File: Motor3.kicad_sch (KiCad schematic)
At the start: 53 parts, among them J601 Step Out, J604 Direction, J605 Direction, Q601 WSF07N10, Q602 WSF07N10, Q603 WSF07N10, Q604 WSF07N10, Q605 WSF07N10, Q606 WSF07N10, Q607 WSF07N10, Q608 WSF07N10

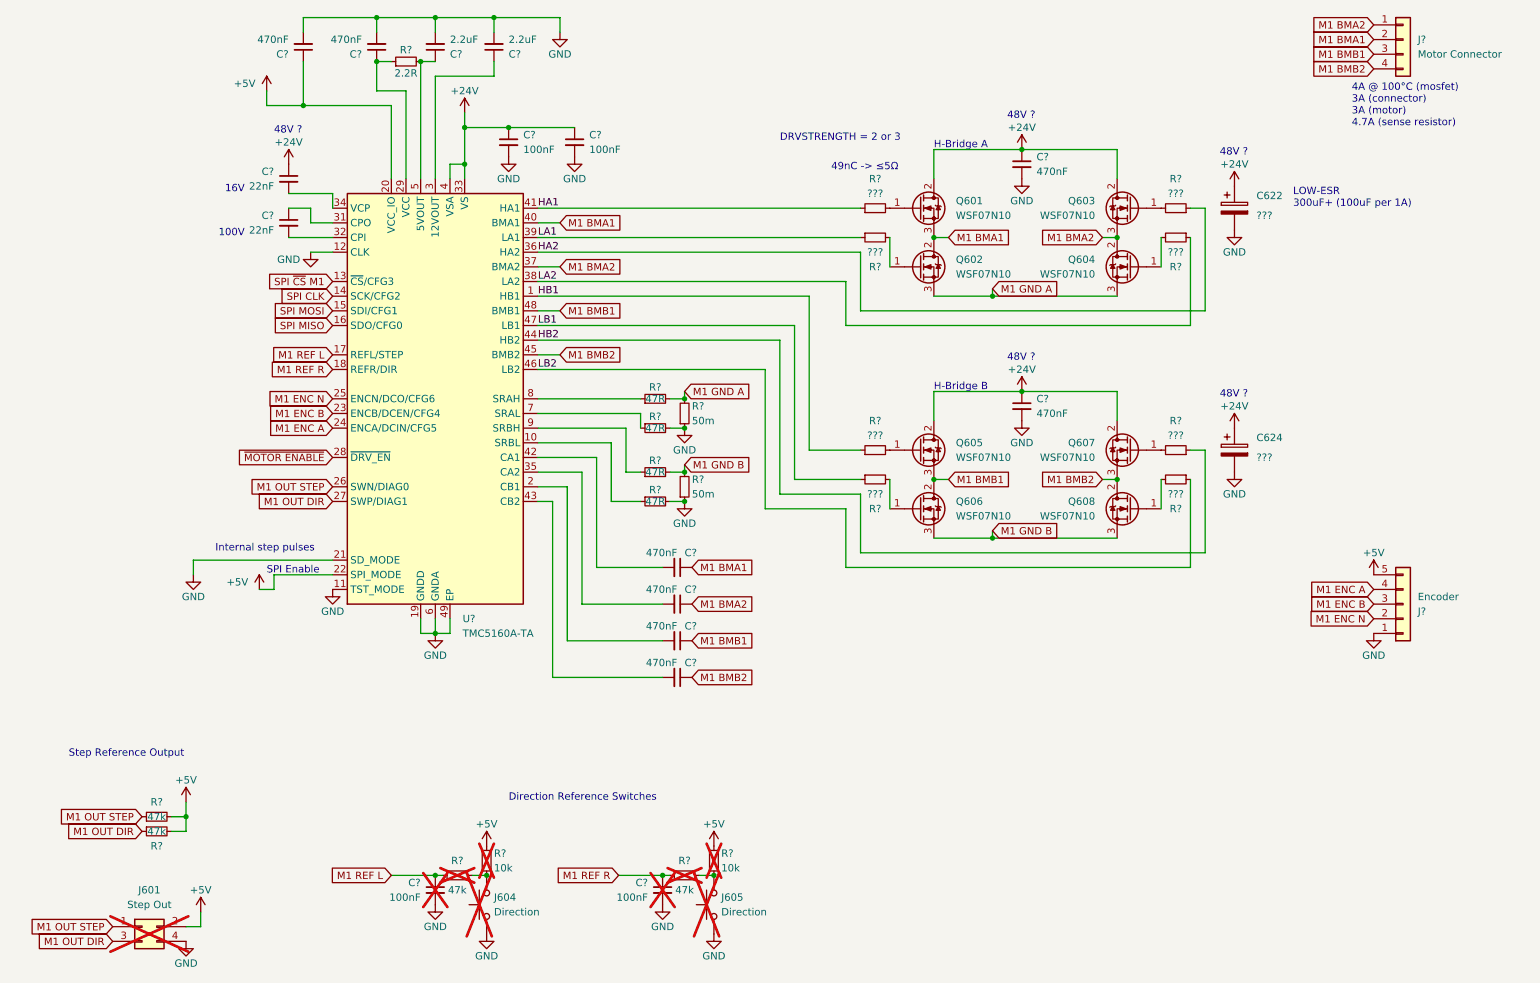
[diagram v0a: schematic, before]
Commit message: Assigning a lot of values to components Change MOSFETS for different (correct) ones Copy Motor1 to Motor2-4 Guess max current per voltage on PowerSupply schema
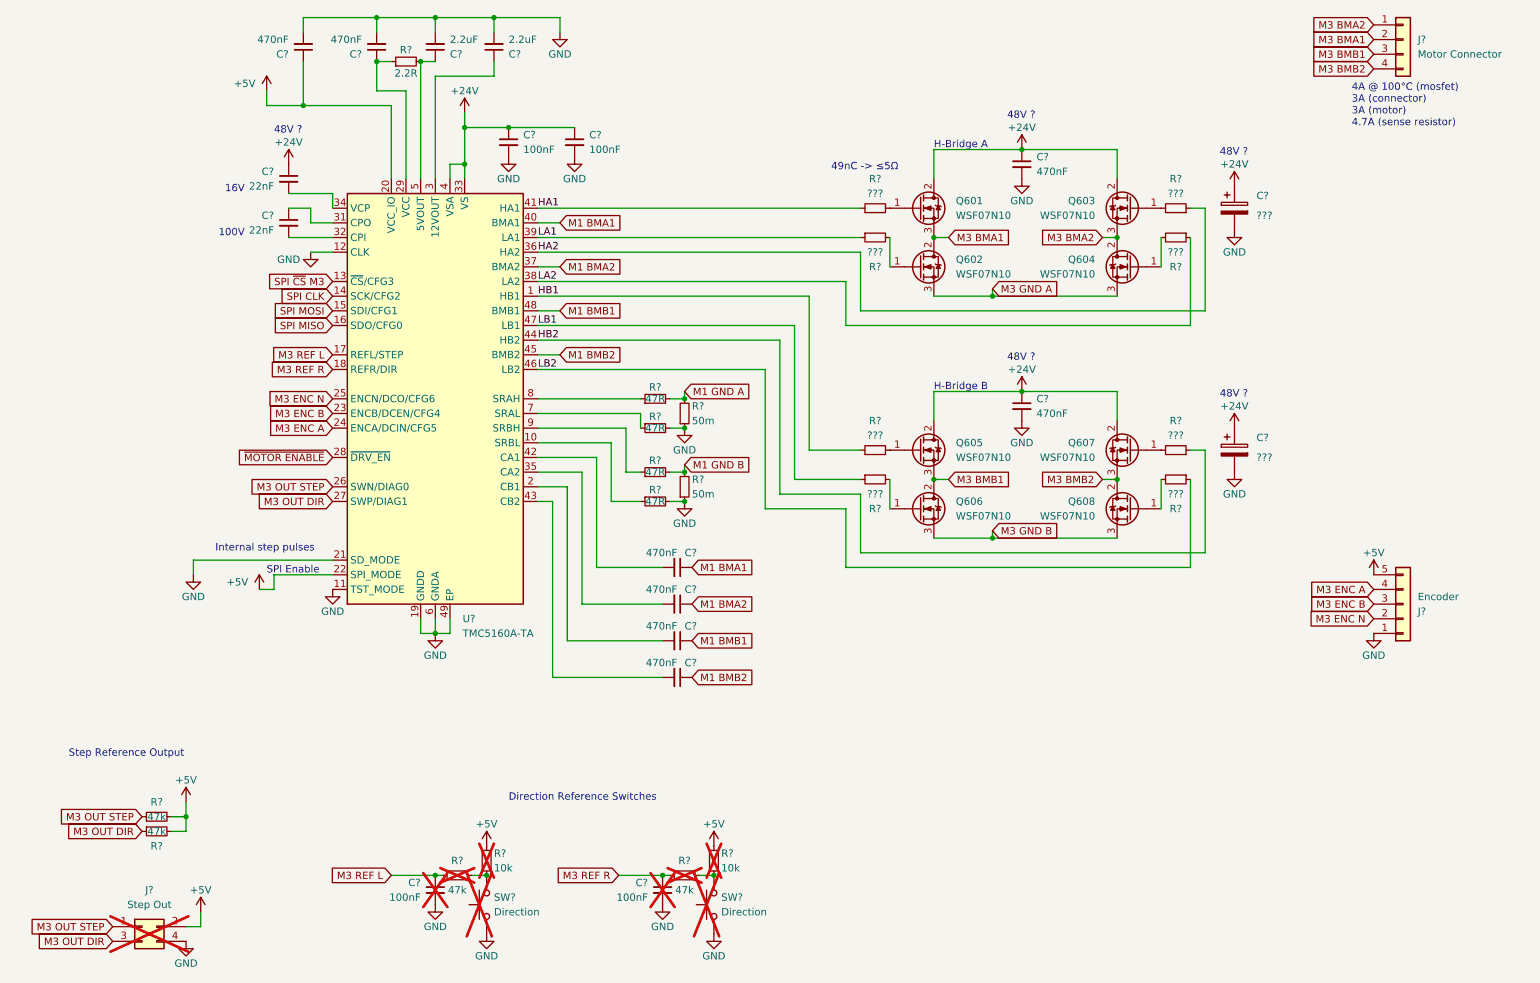
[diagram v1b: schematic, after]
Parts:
- removed C622, C624: ???, symbol Device:C_Polarized
- removed C? (x6): 470nF, Capacitor_SMD:C_1210_3225Metric, symbol Device:C_Small
- removed C? (x4): 100nF, symbol Device:C_Small
- removed C? (x2): 2.2uF, symbol Device:C_Small
- removed C? (x2): 470nF, symbol Device:C_Small
- removed C? (x2): 22nF, symbol Device:C_Small
- removed J601: Step Out, Connector_PinHeader_2.54mm:PinHeader_2x02_P2.54mm_Vertical, symbol Connector_Generic:Conn_02x02_Odd_Even
- removed J604, J605: Direction, Connector_PinHeader_2.54mm:PinHeader_1x02_P2.54mm_Vertical, symbol Switch:SW_Push
- removed J?: Encoder, Connector_JST:JST_XH_B5B-XH-A_1x05_P2.50mm_Vertical, symbol Connector_Generic:Conn_01x05
- removed J?: Motor Connector, Connector_JST:JST_XH_B4B-XH-A_1x04_P2.50mm_Vertical, symbol Connector_Generic:Conn_01x04
- removed R? (x2): 50m, Resistor_SMD:R_2512_6332Metric, symbol Device:R_Small
- removed R? (x4): 47k, symbol Device:R_Small
- removed R? (x8): ???, symbol Device:R_Small
- removed R? (x4): 47R, symbol Device:R_Small
- removed R?: 2.2R, symbol Device:R_Small
- removed R? (x2): 10k, symbol Device:R_Small
- removed U?: TMC5160A-TA, Package_QFP:TQFP-48-1EP_7x7mm_P0.5mm_EP5x5mm_ThermalVias, symbol Driver_Motor:TMC5160A-TA
- added C? (x2): ???, symbol Device:C_Polarized
- added C? (x2): 2.2uF, symbol Device:C_Small
- added C? (x2): 470nF, symbol Device:C_Small
- added C? (x6): 470nF, Capacitor_SMD:C_1210_3225Metric, symbol Device:C_Small
- added C? (x2): 22nF, symbol Device:C_Small
- added C? (x4): 100nF, symbol Device:C_Small
- added J?: Step Out, Connector_PinHeader_2.54mm:PinHeader_2x02_P2.54mm_Vertical, symbol Connector_Generic:Conn_02x02_Odd_Even
- added J?: Encoder, Connector_JST:JST_XH_B5B-XH-A_1x05_P2.50mm_Vertical, symbol Connector_Generic:Conn_01x05
- added J?: Motor Connector, Connector_JST:JST_XH_B4B-XH-A_1x04_P2.50mm_Vertical, symbol Connector_Generic:Conn_01x04
- added R? (x4): 47R, symbol Device:R_Small
- added R? (x4): 47k, symbol Device:R_Small
- added R? (x8): ???, symbol Device:R_Small
- added R? (x2): 50m, Resistor_SMD:R_2512_6332Metric, symbol Device:R_Small
- added R?: 2.2R, symbol Device:R_Small
- added R? (x2): 10k, symbol Device:R_Small
- added SW? (x2): Direction, Connector_PinHeader_2.54mm:PinHeader_1x02_P2.54mm_Vertical, symbol Switch:SW_Push
- added U?: TMC5160A-TA, Package_QFP:TQFP-48-1EP_7x7mm_P0.5mm_EP5x5mm_ThermalVias, symbol Driver_Motor:TMC5160A-TA
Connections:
- net +24V: now also C?.1, C?.1, C?.1, C?.1, C?.1, C?.1, C?.1, U?.33 (VS), U?.4 (VSA)
- net +5V: now also C?.1, J?.2 (Pin_2), J?.5 (Pin_5), R?.2, R?.2, R?.2, R?.2, U?.20 (VCC_IO), U?.22 (SPI_MODE)
- net GND: now also C?.2, C?.2, C?.2, C?.2, C?.2, C?.2, C?.2, C?.2, C?.2, C?.2, C?.2, C?.2, J?.1 (Pin_1), J?.4 (Pin_4), R?.1, R?.1, R?.2, R?.2, SW?.1, SW?.1, U?.11 (TST_MODE), U?.12 (CLK), U?.19 (GNDD), U?.21 (SD_MODE), U?.30 (GNDD), U?.49 (EP), U?.6 (GNDA)
- net HA1: now also R?.1, U?.41 (HA1)
- net HA2: now also R?.1, U?.36 (HA2)
- net HB1: now also R?.1, U?.1 (HB1)
- net HB2: now also R?.1, U?.44 (HB2)
- net LA1: now also R?.1, U?.39 (LA1)
- net LA2: now also R?.1, U?.38 (LA2)
- net LB1: now also R?.1, U?.47 (LB1)
- net LB2: now also R?.1, U?.46 (LB2)
- net M1 BMA1: now also C?.1, U?.40 (BMA1); no longer Q601.3 (S), Q602.2 (D)
- net M1 BMA2: now also C?.1, U?.37 (BMA2); no longer Q603.3 (S), Q604.2 (D)
- net M1 BMB1: now also C?.1, U?.48 (BMB1); no longer Q605.3 (S), Q606.2 (D)
- net M1 BMB2: now also C?.1, U?.45 (BMB2); no longer Q607.3 (S), Q608.2 (D)
- net M1 GND A: now also R?.2, R?.2; no longer Q602.3 (S), Q604.3 (S)
- net M1 GND B: now also R?.2, R?.2; no longer Q606.3 (S), Q608.3 (S)
- net SPI CLK: now also U?.14 (SCK/CFG2)
- net SPI MISO: now also U?.16 (SDO/CFG0)
- net SPI MOSI: now also U?.15 (SDI/CFG1)
- net ~{MOTOR ENABLE}: now also U?.28 (~{DRV_EN})
- net at Q606.1 (G): now also R?.2
- net at Q602.1 (G): now also R?.2
- net at Q608.1 (G): now also R?.2
- net at Q601.1 (G): now also R?.2
- net at Q607.1 (G): now also R?.2
- net at Q603.1 (G): now also R?.2
- net at Q605.1 (G): now also R?.2
- net at Q604.1 (G): now also R?.2
- new net: R?.1, U?.7 (SRAL)
- new net: R?.1, R?.2, SW?.2 (x2)
- new net: R?.1, U?.10 (SRBL)
- new net: C?.2, U?.2 (CB1)
- new net: C?.1, R?.1, U?.29 (VCC)
- new net: C?.1, U?.3 (12VOUT)
- new net: C?.1, U?.31 (CPO)
- new net: C?.2, U?.32 (CPI)
- new net: C?.2, U?.34 (VCP)
- new net: C?.2, U?.35 (CA2)
- new net: C?.2, U?.42 (CA1)
- new net: C?.2, U?.43 (CB2)
- new net: C?.1, R?.2, U?.5 (5VOUT)
- new net: R?.1, U?.8 (SRAH)
- new net: R?.1, U?.9 (SRBH)
- new net M3 BMA1: J?.2 (Pin_2), Q601.3 (S), Q602.2 (D)
- new net M3 BMA2: J?.1 (Pin_1), Q603.3 (S), Q604.2 (D)
- new net M3 BMB1: J?.3 (Pin_3), Q605.3 (S), Q606.2 (D)
- new net M3 BMB2: J?.4 (Pin_4), Q607.3 (S), Q608.2 (D)
- new net M3 ENC A: J?.4 (Pin_4), U?.24 (ENCA/DCIN/CFG5)
- new net M3 ENC B: J?.3 (Pin_3), U?.23 (ENCB/DCEN/CFG4)
- new net M3 ENC N: J?.2 (Pin_2), U?.25 (ENCN/DCO/CFG6)
- new net M3 GND A: Q602.3 (S), Q604.3 (S)
- new net M3 GND B: Q606.3 (S), Q608.3 (S)
- new net M3 OUT DIR: J?.3 (Pin_3), R?.1, U?.27 (SWP/DIAG1)
- new net M3 OUT STEP: J?.1 (Pin_1), R?.1, U?.26 (SWN/DIAG0)
- new net M3 REF L: C?.1, R?.1, U?.17 (REFL/STEP)
- new net M3 REF R: C?.1, R?.1, U?.18 (REFR/DIR)
- new net SPI ~{CS} M3: U?.13 (~{CS}/CFG3)
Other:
- note removed: "DRVSTRENGTH = 2 or 3"
- note removed: "LOW-ESR 300uF+ (100uF per 1A)"
- title: CAN 3D Printer (4 Motor) - Motor 1 -> CAN 3D Printer (4 Motor) - Motor 3

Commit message: Complete schematics Assign every value (very few exceptions) Change TCM5160 from on-board to separate module Add fuses Add power supplies (LDO + 2x buck converter)
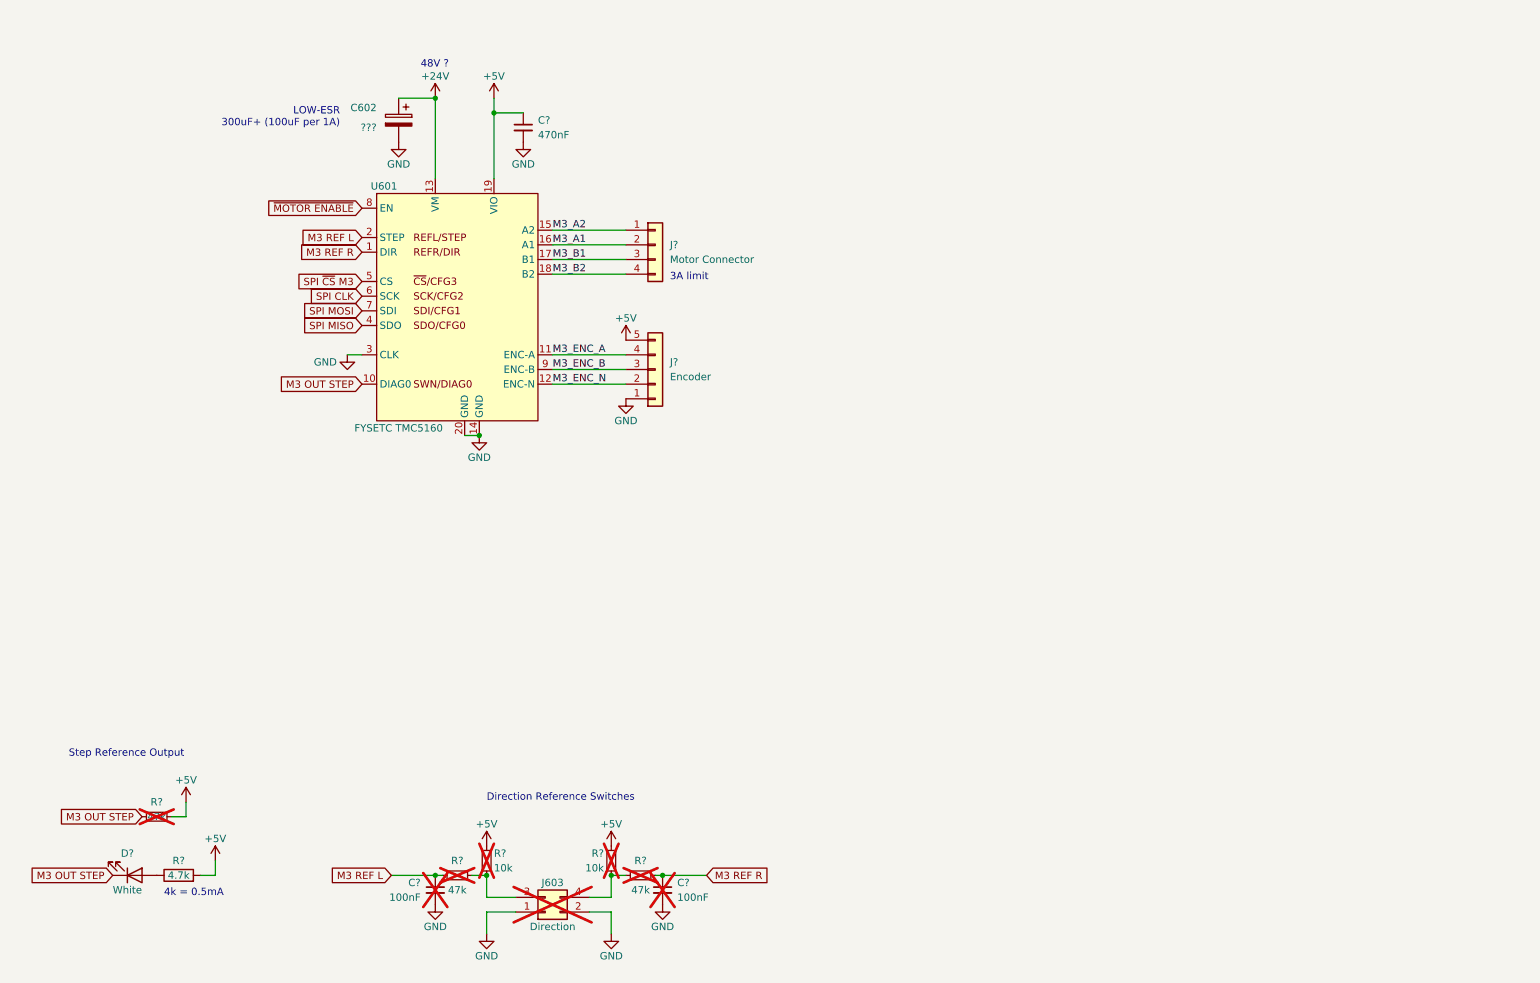
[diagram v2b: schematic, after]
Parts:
- removed C? (x2): ???, symbol Device:C_Polarized
- removed C? (x2): 2.2uF, symbol Device:C_Small
- removed C? (x2): 470nF, symbol Device:C_Small
- removed C? (x6): 470nF, Capacitor_SMD:C_1210_3225Metric, symbol Device:C_Small
- removed C? (x2): 22nF, symbol Device:C_Small
- removed C? (x4): 100nF, symbol Device:C_Small
- removed J?: Step Out, Connector_PinHeader_2.54mm:PinHeader_2x02_P2.54mm_Vertical, symbol Connector_Generic:Conn_02x02_Odd_Even
- removed J?: Encoder, Connector_JST:JST_XH_B5B-XH-A_1x05_P2.50mm_Vertical, symbol Connector_Generic:Conn_01x05
- removed J?: Motor Connector, Connector_JST:JST_XH_B4B-XH-A_1x04_P2.50mm_Vertical, symbol Connector_Generic:Conn_01x04
- removed Q601, Q602, Q603, Q604, Q605, Q606, Q607, Q608: WSF07N10, Package_TO_SOT_SMD:TO-252-2, symbol Transistor_FET:QM6006D
- removed R? (x4): 47R, symbol Device:R_Small
- removed R? (x4): 47k, symbol Device:R_Small
- removed R? (x8): ???, symbol Device:R_Small
- removed R? (x2): 50m, Resistor_SMD:R_2512_6332Metric, symbol Device:R_Small
- removed R?: 2.2R, symbol Device:R_Small
- removed R? (x2): 10k, symbol Device:R_Small
- removed SW? (x2): Direction, Connector_PinHeader_2.54mm:PinHeader_1x02_P2.54mm_Vertical, symbol Switch:SW_Push
- removed U?: TMC5160A-TA, Package_QFP:TQFP-48-1EP_7x7mm_P0.5mm_EP5x5mm_ThermalVias, symbol Driver_Motor:TMC5160A-TA
- added C602: ???, symbol Device:C_Polarized
- added C?: 470nF, Capacitor_SMD:C_0603_1608Metric, symbol Device:C_Small
- added C? (x2): 100nF, Capacitor_SMD:C_0402_1005Metric, symbol Device:C_Small
- added D?: White, LED_SMD:LED_0402_1005Metric, symbol Device:LED
- added J603: Direction, Connector_PinHeader_2.54mm:PinHeader_2x02_P2.54mm_Vertical, symbol Connector_Generic:Conn_02x02_Odd_Even
- added J?: Encoder, Connector_JST:JST_XH_B5B-XH-A_1x05_P2.50mm_Vertical, symbol Connector_Generic:Conn_01x05
- added J?: Motor Connector, Connector_JST:JST_XH_B4B-XH-A_1x04_P2.50mm_Vertical, symbol Connector_Generic:Conn_01x04
- added R? (x2): 10k, Resistor_SMD:R_0603_1608Metric, symbol Device:R_Small
- added R? (x3): 47k, Resistor_SMD:R_0603_1608Metric, symbol Device:R_Small
- added R?: 4.7k, Resistor_SMD:R_0603_1608Metric, symbol Device:R
- added U601: FYSETC TMC5160, Custom:FYSETC TMC5160, symbol Custom:FYSETC_TMC5160
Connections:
- net +24V: now also C602.1, U601.13 (VM)
- net +5V: now also C?.1, J?.5 (Pin_5), R?.2, R?.2, R?.2, R?.2, U601.19 (VIO)
- net GND: now also C602.2, C?.2, C?.2, C?.2, J603.1 (Pin_1), J603.2 (Pin_2), J?.1 (Pin_1), U601.14 (GND), U601.20 (GND), U601.3 (CLK)
- net M3 OUT STEP: now also D?.1 (K), R?.1, U601.10 (DIAG0)
- net M3 REF L: now also C?.1, R?.1, U601.2 (STEP)
- net M3 REF R: now also C?.1, R?.1, U601.1 (DIR)
- net SPI CLK: now also U601.6 (SCK)
- net SPI MISO: now also U601.4 (SDO)
- net SPI MOSI: now also U601.7 (SDI)
- net SPI ~{CS} M3: now also U601.5 (CS)
- net ~{MOTOR ENABLE}: now also U601.8 (EN)
- new net: J603.4 (Pin_4), R?.1, R?.2
- new net: J603.3 (Pin_3), R?.1, R?.2
- new net: D?.2 (A), R?.1
- new net M3_A1: J?.2 (Pin_2), U601.16 (A1)
- new net M3_A2: J?.1 (Pin_1), U601.15 (A2)
- new net M3_B1: J?.3 (Pin_3), U601.17 (B1)
- new net M3_B2: J?.4 (Pin_4), U601.18 (B2)
- new net M3_ENC_A: J?.4 (Pin_4), U601.11 (ENC-A)
- new net M3_ENC_B: J?.3 (Pin_3), U601.9 (ENC-B)
- new net M3_ENC_N: J?.2 (Pin_2), U601.12 (ENC-N)
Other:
- note added: "3A limit"
- note added: "4k = 0.5mA"
- note added: "LOW-ESR 300uF+ (100uF per 1A)"
- note removed: "100V"
- note removed: "16V"
- note removed: "49nC -> ≤5Ω"
- note removed: "4A @ 100°C (mosfet) 3A (connector) 3A (motor) 4.7A (sense resistor)"
- note removed: "H-Bridge A"
- note removed: "H-Bridge B"
- note removed: "Internal step pulses"
- note removed: "SPI Enable"
